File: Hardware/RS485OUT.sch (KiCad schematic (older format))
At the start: 14 parts

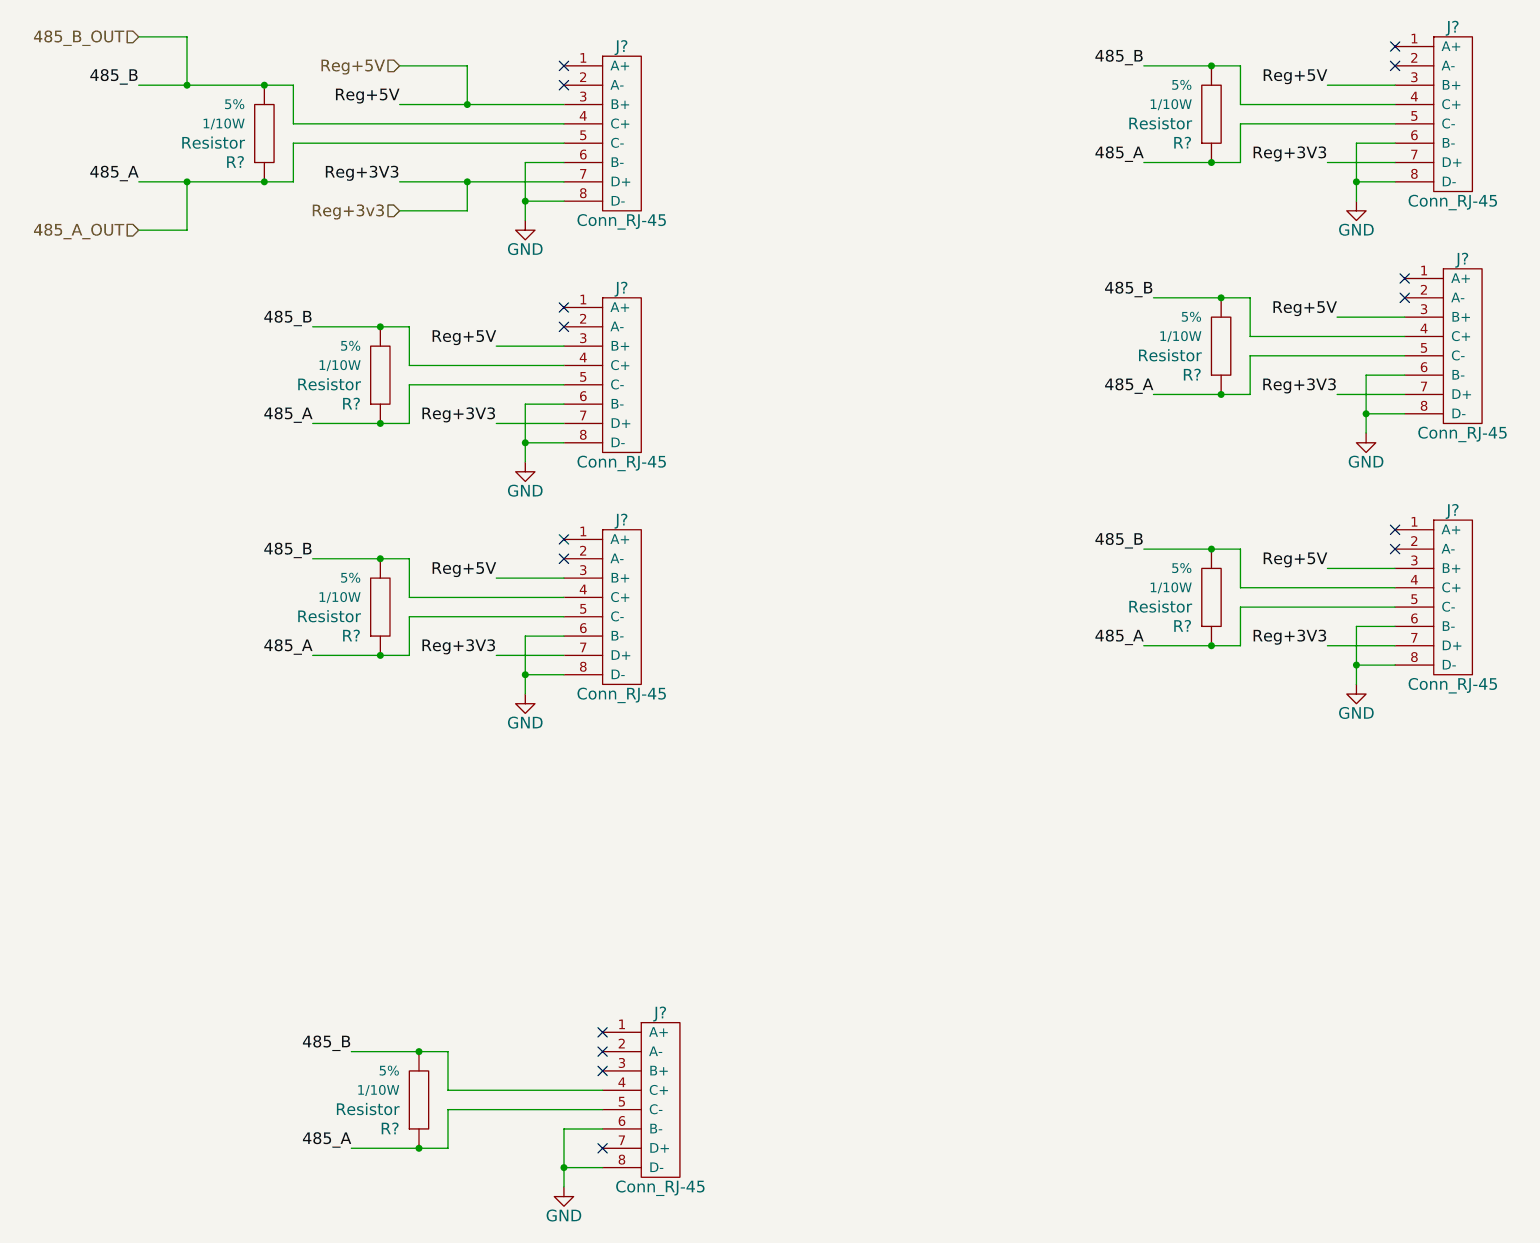
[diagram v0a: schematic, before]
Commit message: Fix capacitor annotation problem
The capacitors from the same library were assigned the same numbers for
an unknown reason.
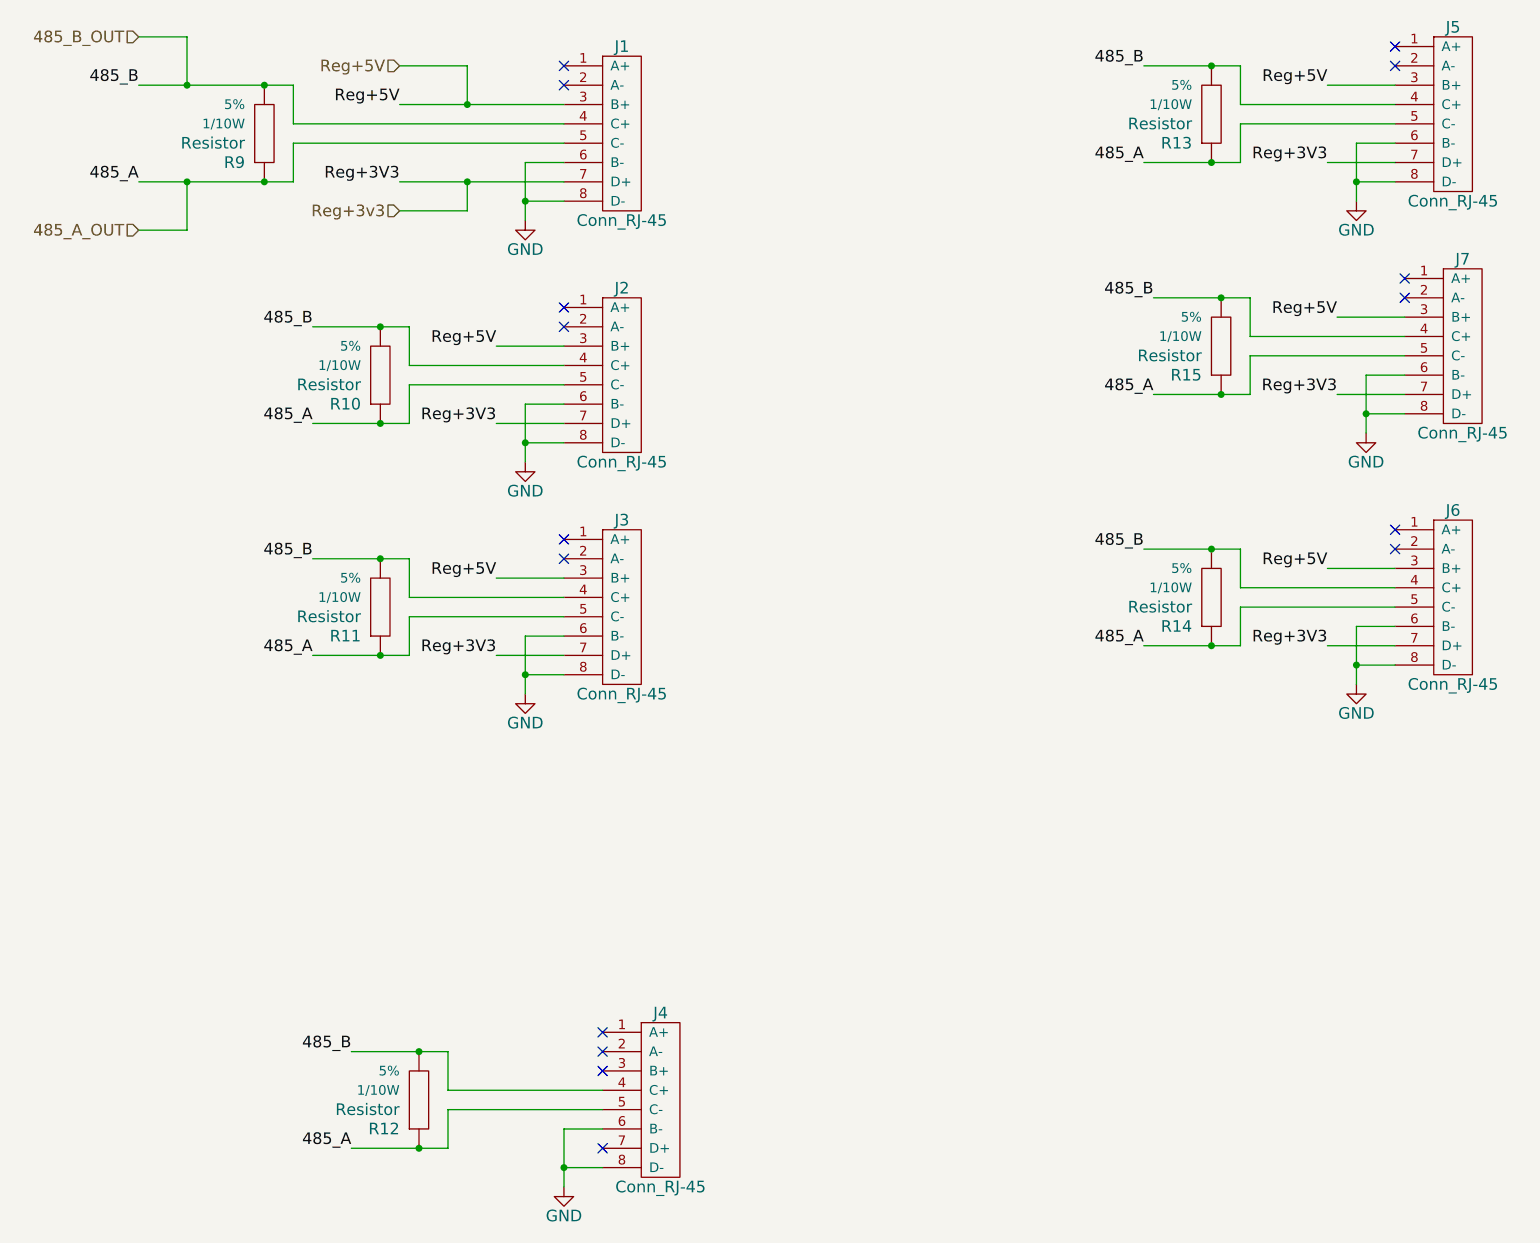
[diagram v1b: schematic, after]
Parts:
- gave numbers to parts that had none: 14
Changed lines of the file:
@@
 $EndDescr
 $Comp
-L Conn_RJ-45 J?
+L Conn_RJ-45 J1
 U 1 1 55205BBA
 P 4800 1250
-F 0 "J?" H 4800 1700 60  0000 C CNN
+F 0 "J1" H 4800 1700 60  0000 C CNN
 F 1 "Conn_RJ-45" H 4800 800 60  0000 C CNN
 F 2 "" H 4800 1550 60  0000 C CNN
@@
 Reg+3V3
 $Comp
-L GND #PWR?
+L GND #PWR21
 U 1 1 55205BC5
 P 4300 1700
-F 0 "#PWR?" H 4300 1450 60  0001 C CNN
+F 0 "#PWR21" H 4300 1450 60  0001 C CNN
 F 1 "GND" H 4300 1550 60  0000 C CNN
 F 2 "" H 4300 1700 60  0000 C CNN
@@
 $EndComp
 $Comp
-L Resistor R?
+L Resistor R9
 U 1 1 55205BD1
 P 2950 1250
-F 0 "R?" V 2800 1350 60  0000 L CNN
+F 0 "R9" V 2800 1350 60  0000 L CNN
 F 1 "Resistor" V 2900 1350 60  0000 L CNN
 F 2 "" H 2850 1250 60  0001 C CNN
@@
 485_A
 $Comp
-L Conn_RJ-45 J?
+L Conn_RJ-45 J2
 U 1 1 55205C70
 P 4800 2500
-F 0 "J?" H 4800 2950 60  0000 C CNN
+F 0 "J2" H 4800 2950 60  0000 C CNN
 F 1 "Conn_RJ-45" H 4800 2050 60  0000 C CNN
 F 2 "" H 4800 2800 60  0000 C CNN
@@
 Reg+3V3
 $Comp
-L GND #PWR?
+L GND #PWR22
 U 1 1 55205C7B
 P 4300 2950
-F 0 "#PWR?" H 4300 2700 60  0001 C CNN
+F 0 "#PWR22" H 4300 2700 60  0001 C CNN
 F 1 "GND" H 4300 2800 60  0000 C CNN
 F 2 "" H 4300 2950 60  0000 C CNN
@@
 $EndComp
 $Comp
-L Resistor R?
+L Resistor R10
 U 1 1 55205C87
 P 3550 2500
-F 0 "R?" V 3400 2600 60  0000 L CNN
+F 0 "R10" V 3400 2600 60  0000 L CNN
 F 1 "Resistor" V 3500 2600 60  0000 L CNN
 F 2 "" H 3450 2500 60  0001 C CNN
@@
 485_A
 $Comp
-L Conn_RJ-45 J?
+L Conn_RJ-45 J3
 U 1 1 55205CF6
 P 4800 3700
-F 0 "J?" H 4800 4150 60  0000 C CNN
+F 0 "J3" H 4800 4150 60  0000 C CNN
 F 1 "Conn_RJ-45" H 4800 3250 60  0000 C CNN
 F 2 "" H 4800 4000 60  0000 C CNN
@@
 Reg+3V3
 $Comp
-L GND #PWR?
+L GND #PWR23
 U 1 1 55205D01
 P 4300 4150
-F 0 "#PWR?" H 4300 3900 60  0001 C CNN
+F 0 "#PWR23" H 4300 3900 60  0001 C CNN
 F 1 "GND" H 4300 4000 60  0000 C CNN
 F 2 "" H 4300 4150 60  0000 C CNN
@@
 $EndComp
 $Comp
-L Resistor R?
+L Resistor R11
 U 1 1 55205D0D
 P 3550 3700
-F 0 "R?" V 3400 3800 60  0000 L CNN
+F 0 "R11" V 3400 3800 60  0000 L CNN
 F 1 "Resistor" V 3500 3800 60  0000 L CNN
 F 2 "" H 3450 3700 60  0001 C CNN
@@
 485_A
 $Comp
-L Conn_RJ-45 J?
+L Conn_RJ-45 J5
 U 1 1 55205D76
 P 9100 1150
-F 0 "J?" H 9100 1600 60  0000 C CNN
+F 0 "J5" H 9100 1600 60  0000 C CNN
 F 1 "Conn_RJ-45" H 9100 700 60  0000 C CNN
 F 2 "" H 9100 1450 60  0000 C CNN
@@
 Reg+3V3
 $Comp
-L GND #PWR?
+L GND #PWR25
 U 1 1 55205D81
 P 8600 1600
-F 0 "#PWR?" H 8600 1350 60  0001 C CNN
+F 0 "#PWR25" H 8600 1350 60  0001 C CNN
 F 1 "GND" H 8600 1450 60  0000 C CNN
 F 2 "" H 8600 1600 60  0000 C CNN
@@
 $EndComp
 $Comp
-L Resistor R?
+L Resistor R13
 U 1 1 55205D8D
 P 7850 1150
-F 0 "R?" V 7700 1250 60  0000 L CNN
+F 0 "R13" V 7700 1250 60  0000 L CNN
 F 1 "Resistor" V 7800 1250 60  0000 L CNN
 F 2 "" H 7750 1150 60  0001 C CNN
@@
 485_A
 $Comp
-L Conn_RJ-45 J?
+L Conn_RJ-45 J7
 U 1 1 55205E04
 P 9150 2350
-F 0 "J?" H 9150 2800 60  0000 C CNN
+F 0 "J7" H 9150 2800 60  0000 C CNN
 F 1 "Conn_RJ-45" H 9150 1900 60  0000 C CNN
 F 2 "" H 9150 2650 60  0000 C CNN
@@
 Reg+3V3
 $Comp
-L GND #PWR?
+L GND #PWR27
 U 1 1 55205E0F
 P 8650 2800
-F 0 "#PWR?" H 8650 2550 60  0001 C CNN
+F 0 "#PWR27" H 8650 2550 60  0001 C CNN
 F 1 "GND" H 8650 2650 60  0000 C CNN
 F 2 "" H 8650 2800 60  0000 C CNN
@@
 $EndComp
 $Comp
-L Resistor R?
+L Resistor R15
 U 1 1 55205E1B
 P 7900 2350
-F 0 "R?" V 7750 2450 60  0000 L CNN
+F 0 "R15" V 7750 2450 60  0000 L CNN
 F 1 "Resistor" V 7850 2450 60  0000 L CNN
 F 2 "" H 7800 2350 60  0001 C CNN
@@
 485_A
 $Comp
-L Conn_RJ-45 J?
+L Conn_RJ-45 J6
 U 1 1 5520604A
 P 9100 3650
-F 0 "J?" H 9100 4100 60  0000 C CNN
+F 0 "J6" H 9100 4100 60  0000 C CNN
 F 1 "Conn_RJ-45" H 9100 3200 60  0000 C CNN
 F 2 "" H 9100 3950 60  0000 C CNN
@@
 Reg+3V3
 $Comp
-L GND #PWR?
+L GND #PWR26
 U 1 1 55206055
 P 8600 4100
-F 0 "#PWR?" H 8600 3850 60  0001 C CNN
+F 0 "#PWR26" H 8600 3850 60  0001 C CNN
 F 1 "GND" H 8600 3950 60  0000 C CNN
 F 2 "" H 8600 4100 60  0000 C CNN
@@
 $EndComp
 $Comp
-L Resistor R?
+L Resistor R14
 U 1 1 55206061
 P 7850 3650
-F 0 "R?" V 7700 3750 60  0000 L CNN
+F 0 "R14" V 7700 3750 60  0000 L CNN
 F 1 "Resistor" V 7800 3750 60  0000 L CNN
 F 2 "" H 7750 3650 60  0001 C CNN
@@
 485_A
 $Comp
-L Conn_RJ-45 J?
+L Conn_RJ-45 J4
 U 1 1 55206120
 P 5000 6250
-F 0 "J?" H 5000 6700 60  0000 C CNN
+F 0 "J4" H 5000 6700 60  0000 C CNN
 F 1 "Conn_RJ-45" H 5000 5800 60  0000 C CNN
 F 2 "" H 5000 6550 60  0000 C CNN
@@
 NoConn ~ 4700 6000
 $Comp
-L GND #PWR?
+L GND #PWR24
 U 1 1 5520612B
 P 4500 6700
-F 0 "#PWR?" H 4500 6450 60  0001 C CNN
+F 0 "#PWR24" H 4500 6450 60  0001 C CNN
 F 1 "GND" H 4500 6550 60  0000 C CNN
 F 2 "" H 4500 6700 60  0000 C CNN
@@
 $EndComp
 $Comp
-L Resistor R?
+L Resistor R12
 U 1 1 55206137
 P 3750 6250
-F 0 "R?" V 3600 6350 60  0000 L CNN
+F 0 "R12" V 3600 6350 60  0000 L CNN
 F 1 "Resistor" V 3700 6350 60  0000 L CNN
 F 2 "" H 3650 6250 60  0001 C CNN

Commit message: Fix annotation problem, Add IC datasheets
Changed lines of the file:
@@
 LIBS:STMicroelectronics
 LIBS:Connectors
+LIBS:74xx
+LIBS:atmel
+LIBS:audio
+LIBS:transistors
 LIBS:Main Board-cache
 EELAYER 25 0
@@
 Reg+3V3
 $Comp
-L GND #PWR21
+L GND #PWR021
 U 1 1 55205BC5
 P 4300 1700
-F 0 "#PWR21" H 4300 1450 60  0001 C CNN
+F 0 "#PWR021" H 4300 1450 60  0001 C CNN
 F 1 "GND" H 4300 1550 60  0000 C CNN
 F 2 "" H 4300 1700 60  0000 C CNN
@@
 Reg+3V3
 $Comp
-L GND #PWR22
+L GND #PWR022
 U 1 1 55205C7B
 P 4300 2950
-F 0 "#PWR22" H 4300 2700 60  0001 C CNN
+F 0 "#PWR022" H 4300 2700 60  0001 C CNN
 F 1 "GND" H 4300 2800 60  0000 C CNN
 F 2 "" H 4300 2950 60  0000 C CNN
@@
 Reg+3V3
 $Comp
-L GND #PWR23
+L GND #PWR023
 U 1 1 55205D01
 P 4300 4150
-F 0 "#PWR23" H 4300 3900 60  0001 C CNN
+F 0 "#PWR023" H 4300 3900 60  0001 C CNN
 F 1 "GND" H 4300 4000 60  0000 C CNN
 F 2 "" H 4300 4150 60  0000 C CNN
@@
 Reg+3V3
 $Comp
-L GND #PWR25
+L GND #PWR024
 U 1 1 55205D81
 P 8600 1600
-F 0 "#PWR25" H 8600 1350 60  0001 C CNN
+F 0 "#PWR024" H 8600 1350 60  0001 C CNN
 F 1 "GND" H 8600 1450 60  0000 C CNN
 F 2 "" H 8600 1600 60  0000 C CNN
@@
 Reg+3V3
 $Comp
-L GND #PWR27
+L GND #PWR025
 U 1 1 55205E0F
 P 8650 2800
-F 0 "#PWR27" H 8650 2550 60  0001 C CNN
+F 0 "#PWR025" H 8650 2550 60  0001 C CNN
 F 1 "GND" H 8650 2650 60  0000 C CNN
 F 2 "" H 8650 2800 60  0000 C CNN
@@
 Reg+3V3
 $Comp
-L GND #PWR26
+L GND #PWR026
 U 1 1 55206055
 P 8600 4100
-F 0 "#PWR26" H 8600 3850 60  0001 C CNN
+F 0 "#PWR026" H 8600 3850 60  0001 C CNN
 F 1 "GND" H 8600 3950 60  0000 C CNN
 F 2 "" H 8600 4100 60  0000 C CNN
@@
 NoConn ~ 4700 6000
 $Comp
-L GND #PWR24
+L GND #PWR027
 U 1 1 5520612B
 P 4500 6700
-F 0 "#PWR24" H 4500 6450 60  0001 C CNN
+F 0 "#PWR027" H 4500 6450 60  0001 C CNN
 F 1 "GND" H 4500 6550 60  0000 C CNN
 F 2 "" H 4500 6700 60  0000 C CNN
@@
 485_A_OUT
 Wire Wire Line
-	4500 1100 4000 1100
-Wire Wire Line
-	4000 1100 3650 1100
+	3650 1100 4500 1100
 Wire Wire Line
 	3100 1200 4500 1200
@@
 	4500 1400 4300 1400
 Wire Wire Line
-	4500 1500 4000 1500
-Wire Wire Line
-	4000 1500 3650 1500
+	3650 1500 4500 1500
 Wire Wire Line
 	4500 1600 4300 1600
 Wire Wire Line
-	4300 1400 4300 1600
-Wire Wire Line
-	4300 1600 4300 1700
+	4300 1400 4300 1700
 Connection ~ 4300 1600
 Wire Wire Line
 	3100 1000 3100 1200
 Wire Wire Line
-	2300 1000 2550 1000
-Wire Wire Line
-	2550 1000 2950 1000
-Wire Wire Line
-	2950 1000 3100 1000
+	2300 1000 3100 1000
 Wire Wire Line
 	3100 1500 3100 1300
 Wire Wire Line
-	2300 1500 2550 1500
-Wire Wire Line
-	2550 1500 2950 1500
-Wire Wire Line
-	2950 1500 3100 1500
+	2300 1500 3100 1500
 Connection ~ 2950 1000
 Connection ~ 2950 1500
@@
 	4500 2850 4300 2850
 Wire Wire Line
-	4300 2650 4300 2850
-Wire Wire Line
-	4300 2850 4300 2950
+	4300 2650 4300 2950
 Connection ~ 4300 2850
 Wire Wire Line
 	3700 2250 3700 2450
 Wire Wire Line
-	3200 2250 3550 2250
-Wire Wire Line
-	3550 2250 3700 2250
+	3200 2250 3700 2250
 Wire Wire Line
 	3700 2750 3700 2550
 Wire Wire Line
-	3200 2750 3550 2750
-Wire Wire Line
-	3550 2750 3700 2750
+	3200 2750 3700 2750
 Connection ~ 3550 2250
 Connection ~ 3550 2750
@@
 	4500 4050 4300 4050
 Wire Wire Line
-	4300 3850 4300 4050
-Wire Wire Line
-	4300 4050 4300 4150
+	4300 3850 4300 4150
 Connection ~ 4300 4050
 Wire Wire Line
 	3700 3450 3700 3650
 Wire Wire Line
-	3200 3450 3550 3450
-Wire Wire Line
-	3550 3450 3700 3450
+	3200 3450 3700 3450
 Wire Wire Line
 	3700 3950 3700 3750
 Wire Wire Line
-	3200 3950 3550 3950
-Wire Wire Line
-	3550 3950 3700 3950
+	3200 3950 3700 3950
 Connection ~ 3550 3450
 Connection ~ 3550 3950
@@
 	8800 1500 8600 1500
 Wire Wire Line
-	8600 1300 8600 1500
-Wire Wire Line
-	8600 1500 8600 1600
+	8600 1300 8600 1600
 Connection ~ 8600 1500
 Wire Wire Line
 	8000 900  8000 1100
 Wire Wire Line
-	7500 900  7850 900
-Wire Wire Line
-	7850 900  8000 900
+	7500 900  8000 900
 Wire Wire Line
 	8000 1400 8000 1200
 Wire Wire Line
-	7500 1400 7850 1400
-Wire Wire Line
-	7850 1400 8000 1400
+	7500 1400 8000 1400
 Connection ~ 7850 900
 Connection ~ 7850 1400
@@
 	8850 2700 8650 2700
 Wire Wire Line
-	8650 2500 8650 2700
-Wire Wire Line
-	8650 2700 8650 2800
+	8650 2500 8650 2800
 Connection ~ 8650 2700
 Wire Wire Line
 	8050 2100 8050 2300
 Wire Wire Line
-	7550 2100 7900 2100
-Wire Wire Line
-	7900 2100 8050 2100
+	7550 2100 8050 2100
 Wire Wire Line
 	8050 2600 8050 2400
 Wire Wire Line
-	7550 2600 7900 2600
-Wire Wire Line
-	7900 2600 8050 2600
+	7550 2600 8050 2600
 Connection ~ 7900 2100
 Connection ~ 7900 2600
@@
 	8800 4000 8600 4000
 Wire Wire Line
-	8600 3800 8600 4000
-Wire Wire Line
-	8600 4000 8600 4100
+	8600 3800 8600 4100
 Connection ~ 8600 4000
 Wire Wire Line
 	8000 3400 8000 3600
 Wire Wire Line
-	7500 3400 7850 3400
-Wire Wire Line
-	7850 3400 8000 3400
+	7500 3400 8000 3400
 Wire Wire Line
 	8000 3900 8000 3700
 Wire Wire Line
-	7500 3900 7850 3900
-Wire Wire Line
-	7850 3900 8000 3900
+	7500 3900 8000 3900
 Connection ~ 7850 3400
 Connection ~ 7850 3900
@@
 	4700 6600 4500 6600
 Wire Wire Line
-	4500 6400 4500 6600
-Wire Wire Line
-	4500 6600 4500 6700
+	4500 6400 4500 6700
 Connection ~ 4500 6600
 Wire Wire Line
 	3900 6000 3900 6200
 Wire Wire Line
-	3400 6000 3750 6000
-Wire Wire Line
-	3750 6000 3900 6000
+	3400 6000 3900 6000
 Wire Wire Line
 	3900 6500 3900 6300
 Wire Wire Line
-	3400 6500 3750 6500
-Wire Wire Line
-	3750 6500 3900 6500
+	3400 6500 3900 6500
 Connection ~ 3750 6000
 Connection ~ 3750 6500
